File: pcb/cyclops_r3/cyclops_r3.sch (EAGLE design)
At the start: 121 parts, among them Q1 BC817-16SMD, Q2 IRF540, U1 MCP4921, U10 MIC5225, U11 AD829, U12 MIC5270, U2 317-N, U3 TLV3701, U4 337-N, U5 ADR03, U6 OP1177, U7 TLV2374, U8 ZXTD45, U9 ADA4899

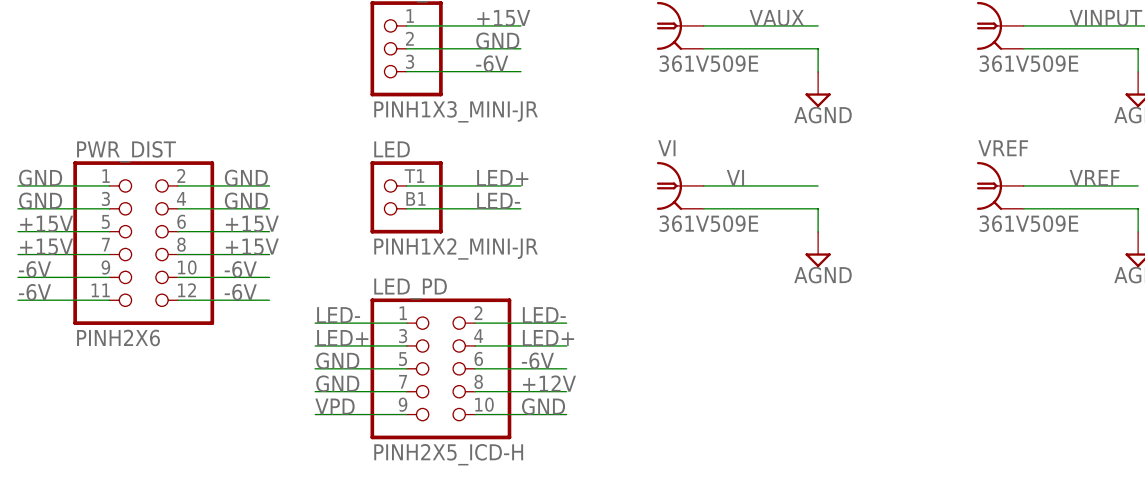
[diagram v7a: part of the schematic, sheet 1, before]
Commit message: Decided the BNC to the PD board is nessesary. Added. Need a 50 ohm coax (video) amp at as the last stage of the PD amp output to drive this line.
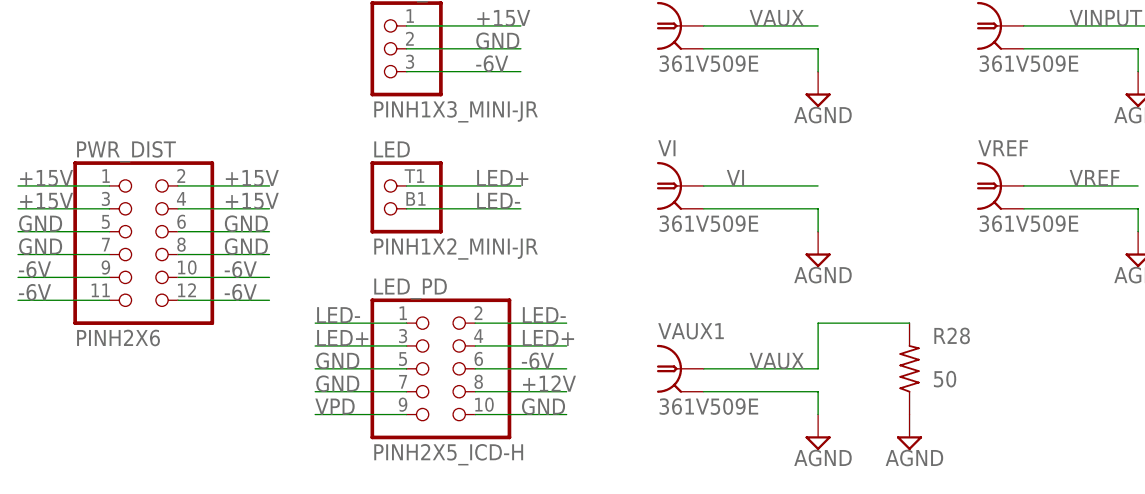
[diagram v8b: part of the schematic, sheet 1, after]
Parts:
- added R28: 50, cyclops:R_0603
- added VAUX1: 361V509E, cyclops:BNC_V-BITE
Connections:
- new net AGND: R28.1
- net +15V: now also PWR_DIST.1, PWR_DIST.2, PWR_DIST.3, PWR_DIST.4; no longer PWR_DIST.5, PWR_DIST.6, PWR_DIST.7, PWR_DIST.8
- net GND: now also PWR_DIST.5, PWR_DIST.6, PWR_DIST.7, PWR_DIST.8, VAUX1.2; no longer PWR_DIST.1, PWR_DIST.2, PWR_DIST.3, PWR_DIST.4
- net VAUX: now also R28.2, VAUX1.1
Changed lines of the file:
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@@
 <part name="P+3" library="cyclops" deviceset="+5V" device=""/>
 <part name="LED_PD" library="cyclops" deviceset="PINH2X5" device="_ICD-H"/>
+<part name="VAUX1" library="cyclops" deviceset="BNC" device="_V-BITE" value="361V509E"/>
+<part name="SUPPLY29" library="cyclops" deviceset="AGND" device=""/>
+<part name="R28" library="cyclops" deviceset="R" device="_0603" value="50"/>
+<part name="SUPPLY32" library="cyclops" deviceset="AGND" device=""/>
 </parts>
 <sheets>
@@
 <instance part="P+3" gate="1" x="73.66" y="0" smashed="yes"/>
 <instance part="LED_PD" gate="G$1" x="68.58" y="-53.34"/>
+<instance part="VAUX1" gate="G$1" x="93.98" y="-53.34"/>
+<instance part="SUPPLY29" gate="G$1" x="109.22" y="-60.96"/>
+<instance part="R28" gate="R" x="119.38" y="-53.34" smashed="yes" rot="R90">
+<attribute name="NAME" x="121.92" y="-50.5714" size="1.778" layer="95"/>
+<attribute name="VALUE" x="121.92" y="-55.372" size="1.778" layer="96"/>
+</instance>
+<instance part="SUPPLY32" gate="G$1" x="119.38" y="-60.96"/>
 </instances>
 <busses>
@@
 </segment>
 <segment>
-<wire x1="30.48" y1="-33.02" x2="20.32" y2="-33.02" width="0.1524" layer="91"/>
-<pinref part="PWR_DIST" gate="G$1" pin="1"/>
-<label x="20.32" y="-33.02" size="1.778" layer="95"/>
-</segment>
-<segment>
-<wire x1="30.48" y1="-35.56" x2="20.32" y2="-35.56" width="0.1524" layer="91"/>
-<pinref part="PWR_DIST" gate="G$1" pin="3"/>
-<label x="20.32" y="-35.56" size="1.778" layer="95"/>
-</segment>
-<segment>
-<wire x1="38.1" y1="-33.02" x2="48.26" y2="-33.02" width="0.1524" layer="91"/>
-<pinref part="PWR_DIST" gate="G$1" pin="2"/>
-<label x="43.18" y="-33.02" size="1.778" layer="95"/>
-</segment>
-<segment>
-<wire x1="38.1" y1="-35.56" x2="48.26" y2="-35.56" width="0.1524" layer="91"/>
-<pinref part="PWR_DIST" gate="G$1" pin="4"/>
-<label x="43.18" y="-35.56" size="1.778" layer="95"/>
-</segment>
-<segment>
 <pinref part="LED_PD" gate="G$1" pin="5"/>
 <wire x1="63.5" y1="-53.34" x2="53.34" y2="-53.34" width="0.1524" layer="91"/>
@@
 <label x="76.2" y="-58.42" size="1.778" layer="95"/>
 </segment>
+<segment>
+<pinref part="VAUX1" gate="G$1" pin="2"/>
+<wire x1="96.52" y1="-55.88" x2="109.22" y2="-55.88" width="0.1524" layer="91"/>
+<wire x1="109.22" y1="-55.88" x2="109.22" y2="-58.42" width="0.1524" layer="91"/>
+<pinref part="SUPPLY29" gate="G$1" pin="AGND"/>
+</segment>
+<segment>
+<wire x1="30.48" y1="-38.1" x2="20.32" y2="-38.1" width="0.1524" layer="91"/>
+<pinref part="PWR_DIST" gate="G$1" pin="5"/>
+<label x="20.32" y="-38.1" size="1.778" layer="95"/>
+</segment>
+<segment>
+<wire x1="30.48" y1="-40.64" x2="20.32" y2="-40.64" width="0.1524" layer="91"/>
+<pinref part="PWR_DIST" gate="G$1" pin="7"/>
+<label x="20.32" y="-40.64" size="1.778" layer="95"/>
+</segment>
+<segment>
+<wire x1="38.1" y1="-40.64" x2="48.26" y2="-40.64" width="0.1524" layer="91"/>
+<pinref part="PWR_DIST" gate="G$1" pin="8"/>
+<label x="43.18" y="-40.64" size="1.778" layer="95"/>
+</segment>
+<segment>
+<wire x1="38.1" y1="-38.1" x2="48.26" y2="-38.1" width="0.1524" layer="91"/>
+<pinref part="PWR_DIST" gate="G$1" pin="6"/>
+<label x="43.18" y="-38.1" size="1.778" layer="95"/>
+</segment>
 </net>
 <net name="VAUX" class="0">
@@
 <wire x1="96.52" y1="-15.24" x2="109.22" y2="-15.24" width="0.1524" layer="91"/>
 <label x="101.6" y="-15.24" size="1.778" layer="95"/>
+</segment>
+<segment>
+<pinref part="VAUX1" gate="G$1" pin="1"/>
+<wire x1="96.52" y1="-53.34" x2="109.22" y2="-53.34" width="0.1524" layer="91"/>
+<label x="101.6" y="-53.34" size="1.778" layer="95"/>
+<wire x1="109.22" y1="-53.34" x2="109.22" y2="-48.26" width="0.1524" layer="91"/>
+<pinref part="R28" gate="R" pin="2"/>
+<wire x1="109.22" y1="-48.26" x2="119.38" y2="-48.26" width="0.1524" layer="91"/>
 </segment>
 </net>
@@
 </segment>
 <segment>
-<wire x1="38.1" y1="-38.1" x2="48.26" y2="-38.1" width="0.1524" layer="91"/>
-<pinref part="PWR_DIST" gate="G$1" pin="6"/>
-<label x="43.18" y="-38.1" size="1.778" layer="95"/>
-</segment>
-<segment>
-<wire x1="38.1" y1="-40.64" x2="48.26" y2="-40.64" width="0.1524" layer="91"/>
-<pinref part="PWR_DIST" gate="G$1" pin="8"/>
-<label x="43.18" y="-40.64" size="1.778" layer="95"/>
-</segment>
-<segment>
-<wire x1="30.48" y1="-40.64" x2="20.32" y2="-40.64" width="0.1524" layer="91"/>
-<pinref part="PWR_DIST" gate="G$1" pin="7"/>
-<label x="20.32" y="-40.64" size="1.778" layer="95"/>
-</segment>
-<segment>
-<wire x1="30.48" y1="-38.1" x2="20.32" y2="-38.1" width="0.1524" layer="91"/>
-<pinref part="PWR_DIST" gate="G$1" pin="5"/>
-<label x="20.32" y="-38.1" size="1.778" layer="95"/>
+<wire x1="30.48" y1="-33.02" x2="20.32" y2="-33.02" width="0.1524" layer="91"/>
+<pinref part="PWR_DIST" gate="G$1" pin="1"/>
+<label x="20.32" y="-33.02" size="1.778" layer="95"/>
+</segment>
+<segment>
+<wire x1="30.48" y1="-35.56" x2="20.32" y2="-35.56" width="0.1524" layer="91"/>
+<pinref part="PWR_DIST" gate="G$1" pin="3"/>
+<label x="20.32" y="-35.56" size="1.778" layer="95"/>
+</segment>
+<segment>
+<wire x1="38.1" y1="-33.02" x2="48.26" y2="-33.02" width="0.1524" layer="91"/>
+<pinref part="PWR_DIST" gate="G$1" pin="2"/>
+<label x="43.18" y="-33.02" size="1.778" layer="95"/>
+</segment>
+<segment>
+<wire x1="38.1" y1="-35.56" x2="48.26" y2="-35.56" width="0.1524" layer="91"/>
+<pinref part="PWR_DIST" gate="G$1" pin="4"/>
+<label x="43.18" y="-35.56" size="1.778" layer="95"/>
 </segment>
 </net>
@@
 </segment>
 </net>
+<net name="AGND" class="0">
+<segment>
+<pinref part="R28" gate="R" pin="1"/>
+<pinref part="SUPPLY32" gate="G$1" pin="AGND"/>
+</segment>
+</net>
